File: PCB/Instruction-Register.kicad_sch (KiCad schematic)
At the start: 23 parts, among them U117 74LS245, U118 74ls245, U119 74LS173

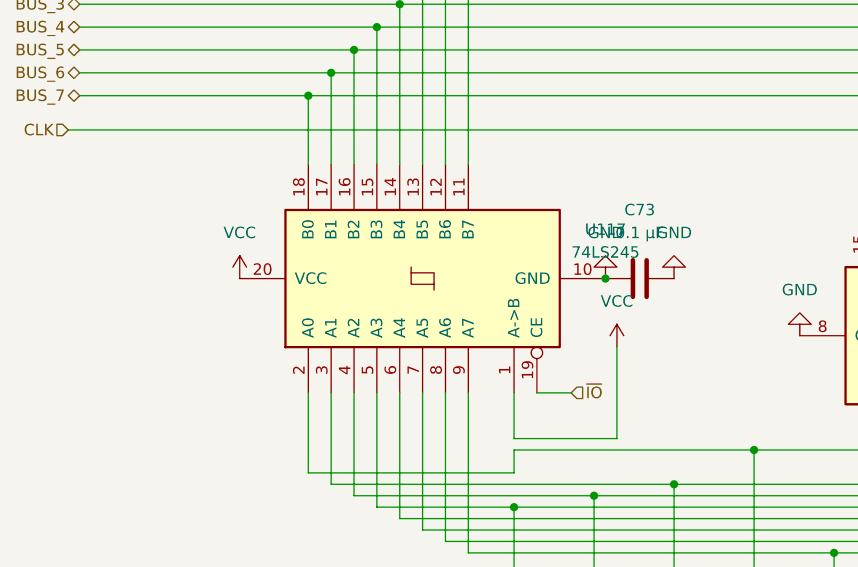
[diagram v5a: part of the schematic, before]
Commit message: updated BOM to match full prices
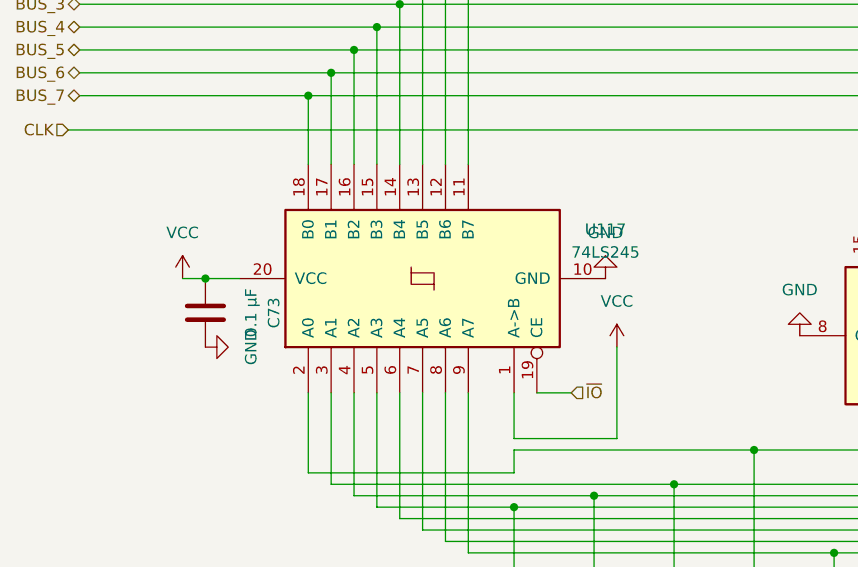
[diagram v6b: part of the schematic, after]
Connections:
- net GND: no longer C73.1
- net VCC: now also C73.1
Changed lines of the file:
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@@
 	)
 	(junction
-		(at 87.63 58.42)
-		(diameter 0)
-		(color 0 0 0 0)
-	)
-	(junction
 		(at 86.36 109.22)
 		(diameter 0)
@@
 	)
 	(junction
+		(at 43.18 58.42)
+		(diameter 0)
+		(color 0 0 0 0)
+	)
+	(junction
 		(at 95.25 133.35)
 		(diameter 0)
@@
 	(wire
 		(pts
+			(xy 43.18 58.42) (xy 46.99 58.42)
+		)
+		(stroke
+			(width 0)
+			(type default)
+		)
+	)
+	(wire
+		(pts
 			(xy 113.03 88.9) (xy 205.74 88.9)
 		)
@@
 	(wire
 		(pts
+			(xy 40.64 58.42) (xy 43.18 58.42)
+		)
+		(stroke
+			(width 0)
+			(type default)
+		)
+	)
+	(wire
+		(pts
 			(xy 205.74 77.47) (xy 205.74 88.9)
 		)
@@
 	)
 	(symbol
-		(lib_id "power:GND")
-		(at 95.25 58.42 180)
-		(unit 1)
-		(exclude_from_sim no)
-		(in_bom yes)
-		(on_board yes)
-		(dnp no)
-		(fields_autoplaced yes)
-		(property "Reference" "#PWR0218"
-			(at 95.25 52.07 0)
-			(effects
-				(font
-					(size 1.27 1.27)
-				)
-				(hide yes)
-			)
-		)
-		(property "Value" "GND"
-			(at 95.25 53.34 0)
-			(effects
-				(font
-					(size 1.27 1.27)
-				)
-			)
-		)
-		(property "Footprint" ""
-			(at 95.25 58.42 0)
-			(effects
-				(font
-					(size 1.27 1.27)
-				)
-				(hide yes)
-			)
-		)
-		(property "Datasheet" ""
-			(at 95.25 58.42 0)
-			(effects
-				(font
-					(size 1.27 1.27)
-				)
-				(hide yes)
-			)
-		)
-		(property "Description" "Power symbol creates a global label with name \"GND\" , ground"
-			(at 95.25 58.42 0)
-			(effects
-				(font
-					(size 1.27 1.27)
-				)
-				(hide yes)
-			)
-		)
-		(pin "1"
-		)
-		(instances
-			(project "8-Bit-PC"
-				(path "/48633dea-2de9-4b6f-aeff-2ee54233f918/039cd62a-c685-4b36-83fd-14086c4f69a9"
-					(reference "#PWR0218")
-					(unit 1)
-				)
-			)
-		)
-	)
-	(symbol
 		(lib_id "Device:R")
 		(at 130.81 129.54 0)
@@
 	)
 	(symbol
+		(lib_id "Device:C")
+		(at 43.18 62.23 0)
+		(unit 1)
+		(exclude_from_sim no)
+		(in_bom yes)
+		(on_board yes)
+		(dnp no)
+		(fields_autoplaced yes)
+		(property "Reference" "C73"
+			(at 50.8 62.23 90)
+			(effects
+				(font
+					(size 1.27 1.27)
+				)
+			)
+		)
+		(property "Value" "0.1 µF"
+			(at 48.26 62.23 90)
+			(effects
+				(font
+					(size 1.27 1.27)
+				)
+			)
+		)
+		(property "Footprint" "Capacitor_THT:C_Radial_D5.0mm_H5.0mm_P2.00mm"
+			(at 44.1452 66.04 0)
+			(effects
+				(font
+					(size 1.27 1.27)
+				)
+				(hide yes)
+			)
+		)
+		(property "Datasheet" "~"
+			(at 43.18 62.23 0)
+			(effects
+				(font
+					(size 1.27 1.27)
+				)
+				(hide yes)
+			)
+		)
+		(property "Description" "Unpolarized capacitor"
+			(at 43.18 62.23 0)
+			(effects
+				(font
+					(size 1.27 1.27)
+				)
+				(hide yes)
+			)
+		)
+		(pin "1"
+		)
+		(pin "2"
+		)
+		(instances
+			(project "8-Bit-PC"
+				(path "/48633dea-2de9-4b6f-aeff-2ee54233f918/039cd62a-c685-4b36-83fd-14086c4f69a9"
+					(reference "C73")
+					(unit 1)
+				)
+			)
+		)
+	)
+	(symbol
 		(lib_id "Device:R")
 		(at 139.7 129.54 0)
@@
 	)
 	(symbol
-		(lib_id "Device:C")
-		(at 91.44 58.42 90)
-		(unit 1)
-		(exclude_from_sim no)
-		(in_bom yes)
-		(on_board yes)
-		(dnp no)
-		(fields_autoplaced yes)
-		(property "Reference" "C73"
-			(at 91.44 50.8 90)
-			(effects
-				(font
-					(size 1.27 1.27)
-				)
-			)
-		)
-		(property "Value" "0.1 µF"
-			(at 91.44 53.34 90)
-			(effects
-				(font
-					(size 1.27 1.27)
-				)
-			)
-		)
-		(property "Footprint" "Capacitor_THT:C_Radial_D5.0mm_H5.0mm_P2.00mm"
-			(at 95.25 57.4548 0)
-			(effects
-				(font
-					(size 1.27 1.27)
-				)
-				(hide yes)
-			)
-		)
-		(property "Datasheet" "~"
-			(at 91.44 58.42 0)
-			(effects
-				(font
-					(size 1.27 1.27)
-				)
-				(hide yes)
-			)
-		)
-		(property "Description" "Unpolarized capacitor"
-			(at 91.44 58.42 0)
-			(effects
-				(font
-					(size 1.27 1.27)
-				)
-				(hide yes)
-			)
-		)
-		(pin "1"
-		)
-		(pin "2"
-		)
-		(instances
-			(project "8-Bit-PC"
-				(path "/48633dea-2de9-4b6f-aeff-2ee54233f918/039cd62a-c685-4b36-83fd-14086c4f69a9"
-					(reference "C73")
-					(unit 1)
-				)
-			)
-		)
-	)
-	(symbol
 		(lib_id "Device:R")
 		(at 86.36 129.54 0)
@@
 	(symbol
 		(lib_id "power:VCC")
-		(at 46.99 58.42 0)
+		(at 40.64 58.42 0)
 		(unit 1)
 		(exclude_from_sim no)
@@
 		(fields_autoplaced yes)
 		(property "Reference" "#PWR0140"
-			(at 46.99 62.23 0)
+			(at 40.64 62.23 0)
 			(effects
 				(font
@@
 		)
 		(property "Value" "VCC"
-			(at 46.99 53.34 0)
+			(at 40.64 53.34 0)
 			(effects
 				(font
@@
 		)
 		(property "Footprint" ""
-			(at 46.99 58.42 0)
+			(at 40.64 58.42 0)
 			(effects
 				(font
@@
 		)
 		(property "Datasheet" ""
-			(at 46.99 58.42 0)
+			(at 40.64 58.42 0)
 			(effects
 				(font
@@
 		)
 		(property "Description" "Power symbol creates a global label with name \"VCC\""
-			(at 46.99 58.42 0)
+			(at 40.64 58.42 0)
 			(effects
 				(font
@@
 					(unit 1)
 				)
+			)
+		)
+	)
+	(symbol
+		(lib_id "power:GND")
+		(at 43.18 66.04 90)
+		(unit 1)
+		(exclude_from_sim no)
+		(in_bom yes)
+		(on_board yes)
+		(dnp no)
+		(fields_autoplaced yes)
+		(property "Reference" "#PWR0218"
+			(at 49.53 66.04 0)
+			(effects
+				(font
+					(size 1.27 1.27)
+				)
+				(hide yes)
+			)
+		)
+		(property "Value" "GND"
+			(at 48.26 66.04 0)
+			(effects
+				(font
+					(size 1.27 1.27)
+				)
+			)
+		)
+		(property "Footprint" ""
+			(at 43.18 66.04 0)
+			(effects
+				(font
+					(size 1.27 1.27)
+				)
+				(hide yes)
+			)
+		)
+		(property "Datasheet" ""
+			(at 43.18 66.04 0)
+			(effects
+				(font
+					(size 1.27 1.27)
+				)
+				(hide yes)
+			)
+		)
+		(property "Description" "Power symbol creates a global label with name \"GND\" , ground"
+			(at 43.18 66.04 0)
+			(effects
+				(font
+					(size 1.27 1.27)
+				)
+				(hide yes)
+			)
+		)
+		(pin "1"
+		)
+		(instances
+			(project "8-Bit-PC"
+				(path "/48633dea-2de9-4b6f-aeff-2ee54233f918/039cd62a-c685-4b36-83fd-14086c4f69a9"
+					(reference "#PWR0218")
+					(unit 1)
+				)

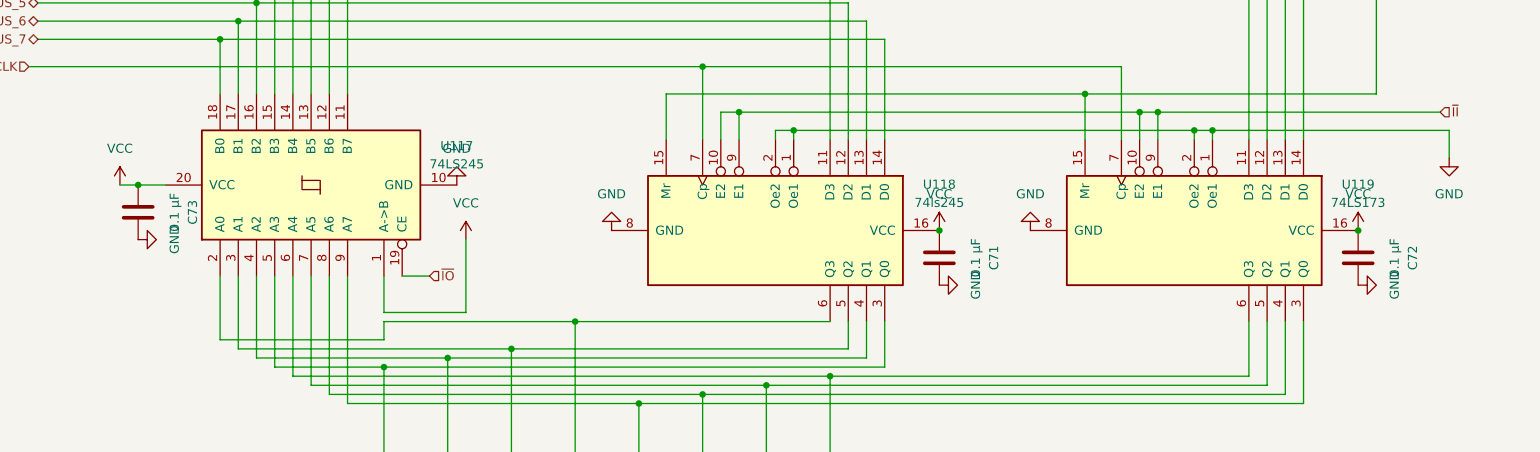
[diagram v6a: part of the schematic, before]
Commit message: Redoing PCB layout and fixed some signal flow convention errors
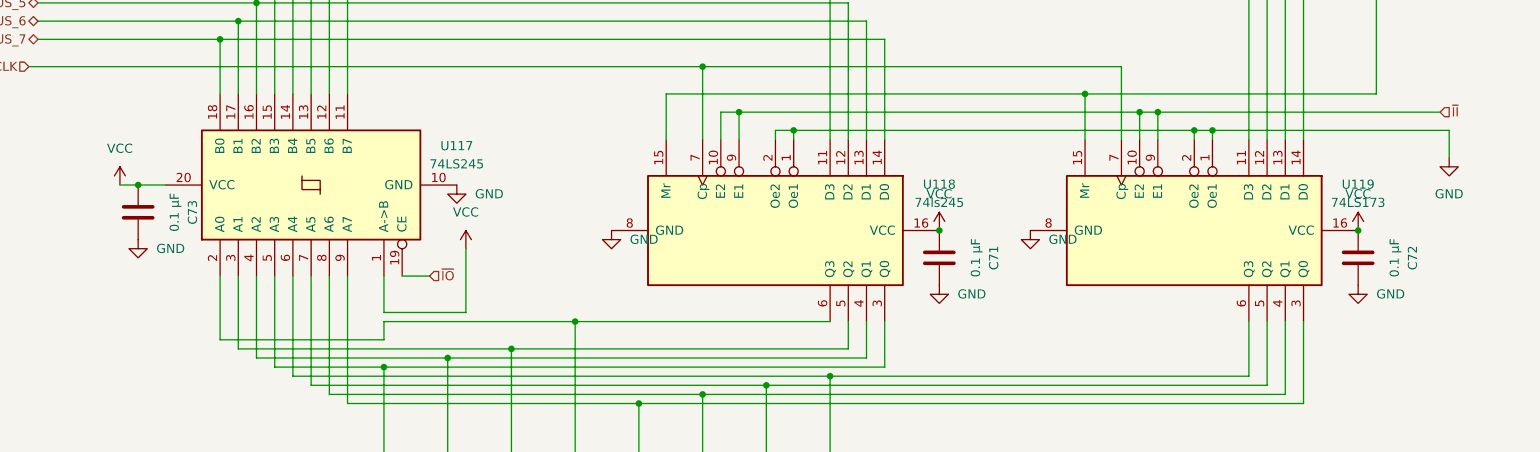
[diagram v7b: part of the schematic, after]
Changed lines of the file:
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@@
 	(wire
 		(pts
-			(xy 88.9 76.2) (xy 88.9 66.04)
+			(xy 88.9 76.2) (xy 88.9 67.31)
 		)
 		(stroke
@@
 	(symbol
 		(lib_id "power:GND")
-		(at 87.63 58.42 180)
+		(at 87.63 58.42 0)
 		(unit 1)
 		(exclude_from_sim no)
@@
 		(fields_autoplaced yes)
 		(property "Reference" "#PWR0143"
-			(at 87.63 52.07 0)
+			(at 87.63 64.77 0)
 			(effects
 				(font
@@
 		)
 		(property "Value" "GND"
-			(at 87.63 53.34 0)
-			(effects
-				(font
-					(size 1.27 1.27)
-				)
+			(at 90.17 59.6899 0)
+			(effects
+				(font
+					(size 1.27 1.27)
+				)
+				(justify left)
 			)
 		)
@@
 	(symbol
 		(lib_id "power:VCC")
-		(at 88.9 66.04 0)
+		(at 88.9 67.31 0)
 		(unit 1)
 		(exclude_from_sim no)
@@
 		(fields_autoplaced yes)
 		(property "Reference" "#PWR0110"
-			(at 88.9 69.85 0)
+			(at 88.9 71.12 0)
 			(effects
 				(font
@@
 		)
 		(property "Value" "VCC"
-			(at 88.9 60.96 0)
+			(at 88.9 62.23 0)
 			(effects
 				(font
@@
 		)
 		(property "Footprint" ""
-			(at 88.9 66.04 0)
+			(at 88.9 67.31 0)
 			(effects
 				(font
@@
 		)
 		(property "Datasheet" ""
-			(at 88.9 66.04 0)
+			(at 88.9 67.31 0)
 			(effects
 				(font
@@
 		)
 		(property "Description" "Power symbol creates a global label with name \"VCC\""
-			(at 88.9 66.04 0)
+			(at 88.9 67.31 0)
 			(effects
 				(font
@@
 	(symbol
 		(lib_id "power:GND")
-		(at 213.36 72.39 90)
+		(at 213.36 72.39 0)
 		(unit 1)
 		(exclude_from_sim no)
@@
 		(fields_autoplaced yes)
 		(property "Reference" "#PWR0217"
-			(at 219.71 72.39 0)
+			(at 213.36 78.74 0)
 			(effects
 				(font
@@
 		)
 		(property "Value" "GND"
-			(at 218.44 72.39 0)
-			(effects
-				(font
-					(size 1.27 1.27)
-				)
+			(at 215.9 73.6599 0)
+			(effects
+				(font
+					(size 1.27 1.27)
+				)
+				(justify left)
 			)
 		)
@@
 	(symbol
 		(lib_id "power:GND")
-		(at 167.64 64.77 180)
+		(at 167.64 64.77 0)
 		(unit 1)
 		(exclude_from_sim no)
@@
 		(fields_autoplaced yes)
 		(property "Reference" "#PWR0145"
-			(at 167.64 58.42 0)
+			(at 167.64 71.12 0)
 			(effects
 				(font
@@
 		)
 		(property "Value" "GND"
-			(at 167.64 59.69 0)
-			(effects
-				(font
-					(size 1.27 1.27)
-				)
+			(at 170.18 66.0399 0)
+			(effects
+				(font
+					(size 1.27 1.27)
+				)
+				(justify left)
 			)
 		)
@@
 	(symbol
 		(lib_id "power:GND")
-		(at 109.22 64.77 180)
+		(at 109.22 64.77 0)
 		(unit 1)
 		(exclude_from_sim no)
@@
 		(fields_autoplaced yes)
 		(property "Reference" "#PWR0144"
-			(at 109.22 58.42 0)
+			(at 109.22 71.12 0)
 			(effects
 				(font
@@
 		)
 		(property "Value" "GND"
-			(at 109.22 59.69 0)
-			(effects
-				(font
-					(size 1.27 1.27)
-				)
+			(at 111.76 66.0399 0)
+			(effects
+				(font
+					(size 1.27 1.27)
+				)
+				(justify left)
 			)
 		)
@@
 	(symbol
 		(lib_id "power:GND")
-		(at 43.18 66.04 90)
+		(at 43.18 66.04 0)
 		(unit 1)
 		(exclude_from_sim no)
@@
 		(fields_autoplaced yes)
 		(property "Reference" "#PWR0218"
-			(at 49.53 66.04 0)
+			(at 43.18 72.39 0)
 			(effects
 				(font
@@
 		)
 		(property "Value" "GND"
-			(at 48.26 66.04 0)
-			(effects
-				(font
-					(size 1.27 1.27)
-				)
+			(at 45.72 67.3099 0)
+			(effects
+				(font
+					(size 1.27 1.27)
+				)
+				(justify left)
 			)
 		)
@@
 	(symbol
 		(lib_id "power:GND")
-		(at 154.94 72.39 90)
+		(at 154.94 72.39 0)
 		(unit 1)
 		(exclude_from_sim no)
@@
 		(fields_autoplaced yes)
 		(property "Reference" "#PWR0216"
-			(at 161.29 72.39 0)
+			(at 154.94 78.74 0)
 			(effects
 				(font
@@
 		)
 		(property "Value" "GND"
-			(at 160.02 72.39 0)
-			(effects
-				(font
-					(size 1.27 1.27)
-				)
-			)
-		)
+			(at 157.48 73.6599 0)
+			(effects
+				(font
+					(size 1.27 1.27)
+				)
+				(justify left)
+			)
+		)
